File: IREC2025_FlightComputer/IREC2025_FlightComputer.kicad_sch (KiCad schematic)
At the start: 66 parts, among them J1 Molex Microfit, J2 BOOT0, J4 Conn_02x03_Counter_Clockwise, Q1 SI7232DN-T1-GE3, U1 STM32U575VGTx, U2 NRVB120VLSFT1G, U4 NRVB120VLSFT1G, U5 LP5912Q3.3DRVRQ1, U8 TPS62153, U9 SN74HCT125DR, X1 1XXD32000MBA

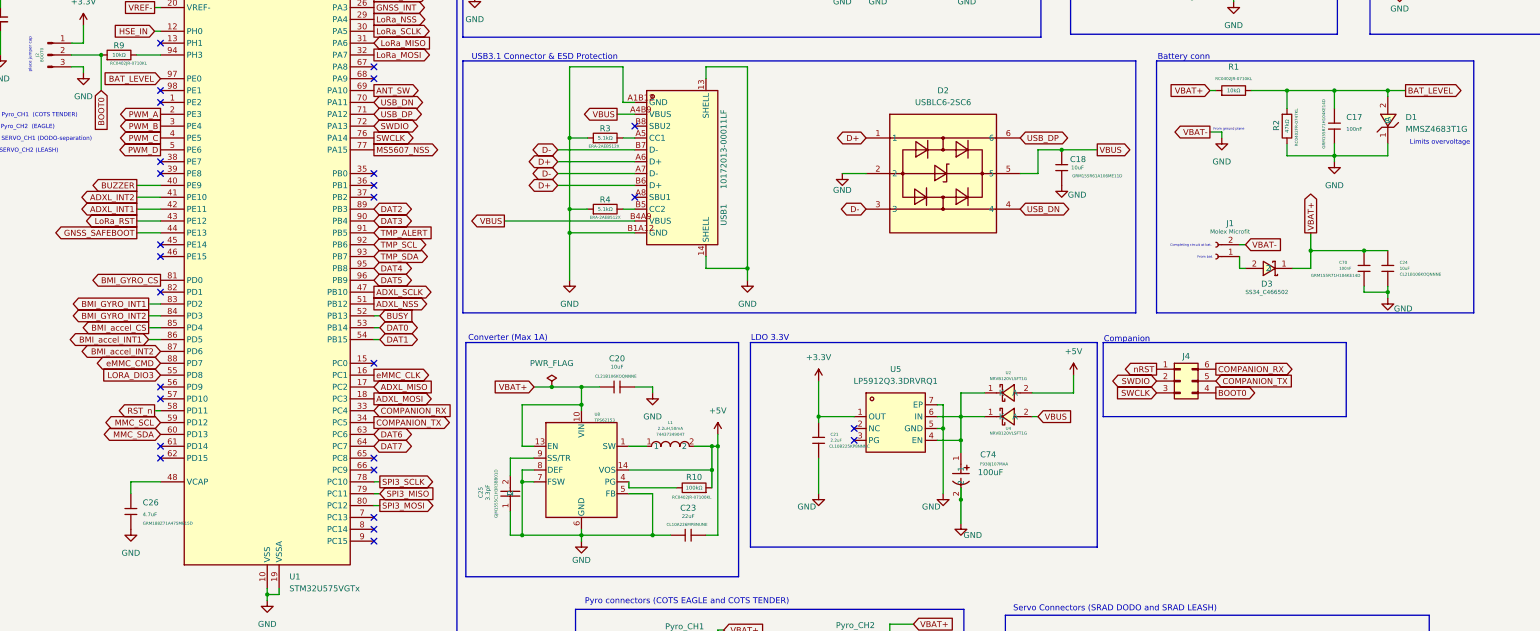
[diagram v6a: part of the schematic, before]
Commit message: Layout change
Layout changes (Particularly GNSS and LoRa)
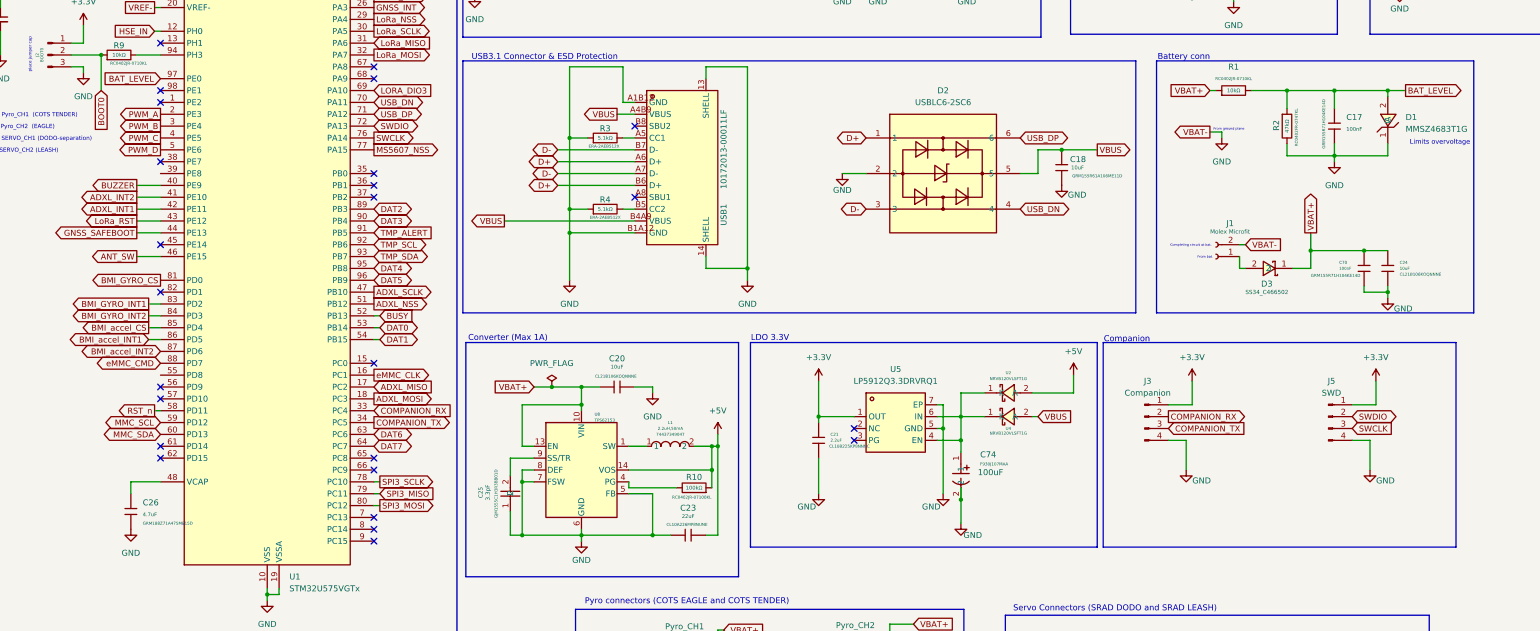
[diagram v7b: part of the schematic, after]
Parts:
- removed J4: Conn_02x03_Counter_Clockwise, Connector_PinHeader_2.54mm:PinHeader_2x03_P2.54mm_Vertical, symbol Connector_Generic:Conn_02x03_Counter_Clockwise
- added J3: Companion, Connector_PinHeader_2.54mm:PinHeader_1x04_P2.54mm_Vertical, symbol Connector:Conn_01x04_Pin
- added J5: SWD, Connector_PinHeader_2.54mm:PinHeader_1x04_P2.54mm_Vertical, symbol Connector:Conn_01x04_Pin
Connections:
- net +3.3V: now also J3.1 (Pin_1), J5.1 (Pin_1)
- net ANT_SW: now also U1.46 (PE15); no longer U1.69 (PA10)
- net COMPANION_RX: now also J3.2 (Pin_2)
- net COMPANION_TX: now also J3.3 (Pin_3)
- net GND: now also J3.4 (Pin_4), J5.4 (Pin_4)
- net LORA_DIO3: now also U1.69 (PA10); no longer U1.55 (PD8)
- net SWCLK: now also J5.3 (Pin_3)
- net SWDIO: now also J5.2 (Pin_2)
- no-connect marks 27 -> 25

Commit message: small fixes
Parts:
- added LED3: HS-0402-UR, EasyEDA:LED0402-R-RD, symbol EasyEDA:HS-0402-UR
- added R39: 1kΩ, PCM_JLCPCB:R_0402, symbol PCM_JLCPCB-Resistors:0402,1kΩ
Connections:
- net +3.3V: now also LED3.1 (+)
- net GND: now also R39.1
- new net: LED3.2 (-), R39.2
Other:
- moved on the sheet: C21
